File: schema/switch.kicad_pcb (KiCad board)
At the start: 2 copper layers, 48 parts, among them IC1 ATMEGA8A-A, K1 RT424F05, K2 RT424F05, P1 12v-gnd-clunet, P10 Gnd, P11 R1_, P12 R2_, P13 R1_, P14 R2_, P15 CON_MIS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

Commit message: Изменил тактовые кнопки на датчики Холла
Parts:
- removed SW1, SW2, SW3: Sw1, Buttons_Switches_SMD:SW_SPST_PTS645
- added D4: AH201, TO_SOT_Packages_THT:TO-92_Inline_Wide, F.Cu at (111.1, 114.0)
- added D5: AH201, TO_SOT_Packages_THT:TO-92_Inline_Wide, F.Cu at (132.5, 114.0)
- added D6: AH201, TO_SOT_Packages_THT:TO-92_Inline_Wide, F.Cu at (148.9, 114.0)
- moved R4 2.60 mm to (119.4, 104.4)
- moved R2 2.50 mm to (116.1, 107.1)
- moved P16 1.42 mm to (127.0, 108.5)
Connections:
- P20 pad 1: Net-(P20-Pad1) -> +5V
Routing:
- net VCC: track 63.0 -> 152.8 mm
- net GND: track 170.0 -> 152.9 mm
- net +5V: track 49.6 -> 60.8 mm
- net /SW2: track 30.8 -> 24.7 mm
- net /SW3: track 30.4 -> 24.6 mm
- net /SW1: track 36.4 -> 30.9 mm
- net /LED1_2: track 19.2 -> 16.5 mm
- net /LED1_1: track 24.0 -> 21.5 mm
- net /LED2_1: track 15.8 -> 17.1 mm
- net Net-(D1-Pad3): track 4.71 -> 5.79 mm
- net Net-(D1-Pad1): track 7.57 -> 8.51 mm

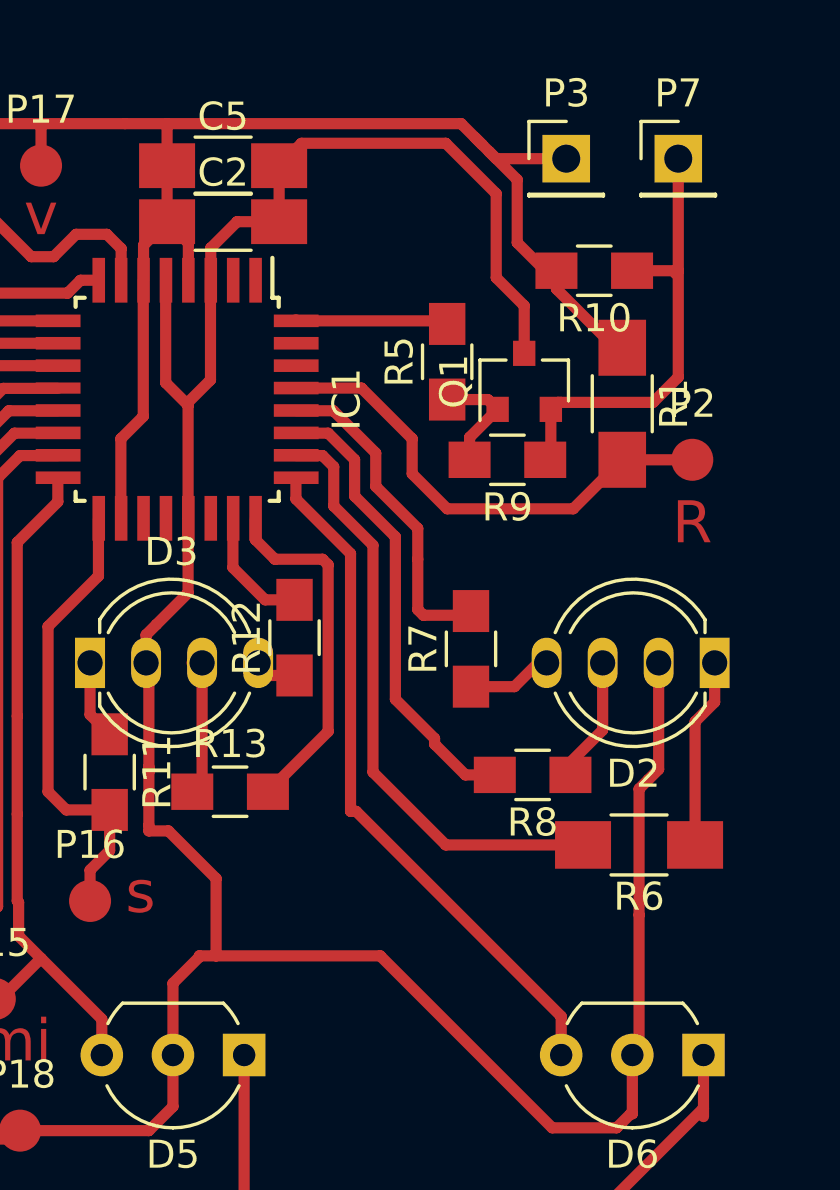
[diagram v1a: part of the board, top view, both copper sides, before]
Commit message: Добавление крышки
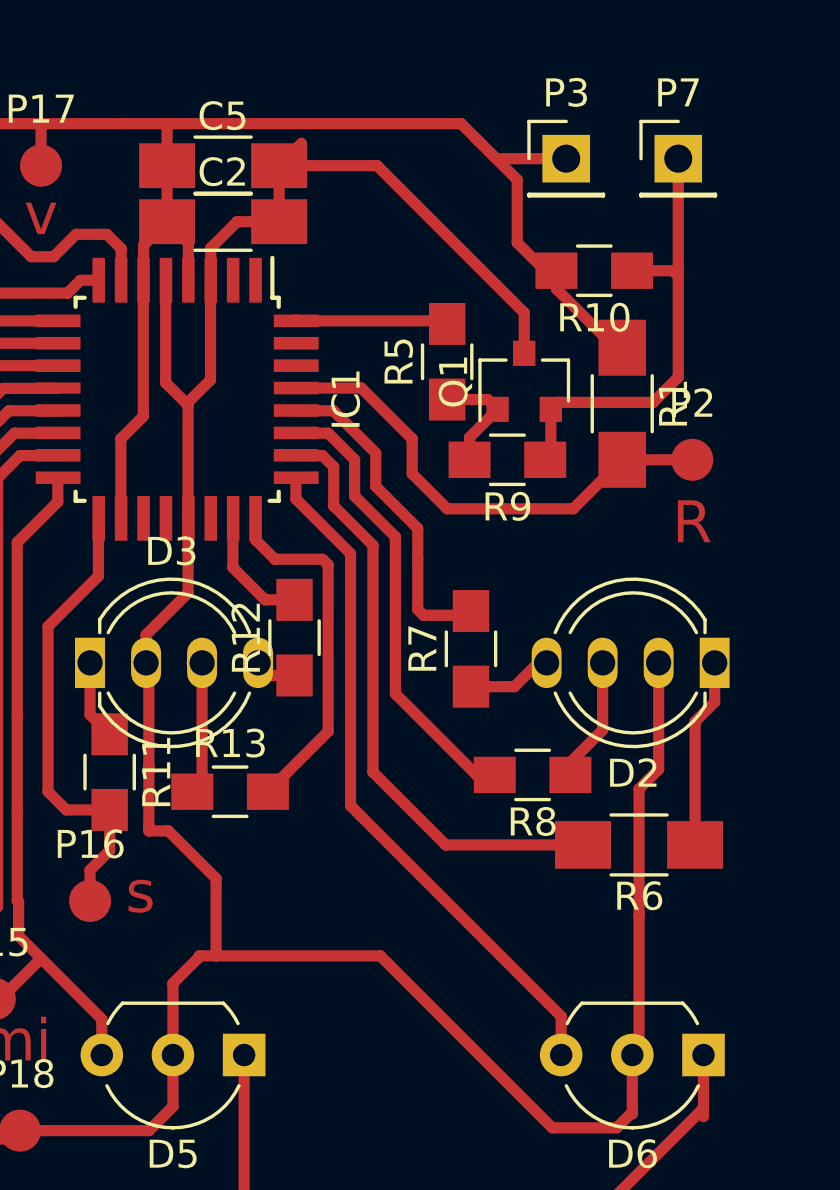
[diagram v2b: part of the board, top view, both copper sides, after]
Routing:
- net GND: track 152.9 -> 151.4 mm
